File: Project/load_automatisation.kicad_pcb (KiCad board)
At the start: 2 copper layers, 263.4 x 251.4 mm, 115 parts, among them IC1 OPA2145IDR, IC10 TD62083AFGNEL, IC11 MC74VHC138DR2G, IC2 TD62083AFGNEL, IC3 TD62083AFGNEL, IC4 MC74VHC138DR2G, IC5 MC74VHC138DR2G, IC6 TD62083AFGNEL, IC7 TD62083AFGNEL, IC8 TD62083AFGNEL, IC9 OPA145IDBVT, J1 PowerNeg, J12 PH-2X05SG, J13 1757242, J30 1757349, J9 PowerIn, K1 V23079C1103B301, K10 IMC03TS, K11 V23079C1103B301, K12 V23079C1103B301, K13 V23079C1103B301, K14 IMC03TS, K15 IMC03TS, K16 IMC03TS, K17 V23079C1103B301, K18 V23079C1103B301, K19 V23079C1103B301, K2 V23079C1103B301, K20 V23079C1103B301, K21 V23079C1103B301, K22 IMC03TS, K23 IMC03TS, K24 IMC03TS, K25 IMC03TS, K26 IMC03TS, K27 V23079C1103B301, K28 V23079C1103B301, K29 V23079C1103B301, K3 V23079C1103B301, K30 IMC03TS, K31 IMC03TS, K32 IMC03TS, K33 V23079C1103B301, K34 V23079C1103B301, K35 V23079C1103B301, K36 V23079C1103B301, K37 V23079C1103B301, K38 IMC03TS, K39 IMC03TS, K4 V23079C1103B301, K40 IMC03TS, K41 IMC03TS, K42 IMC03TS, K43 V23079C1103B301, K44 V23079C1103B301, K45 V23079C1103B301, K46 IMC03TS, K47 IMC03TS, K48 IMC03TS, K5 V23079C1103B301, K6 IMC03TS, K7 IMC03TS, K8 IMC03TS, K9 IMC03TS, U1 AMS1117-5.0, U2 INA128, U3 AMS1117-5.0

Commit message: place arrangement
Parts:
- added C17: 100nF, Capacitor_SMD:C_0805_2012Metric, F.Cu at (197.2, 158.9)
- added C18: 100nF, Capacitor_SMD:C_0805_2012Metric, F.Cu at (192.3, 178.8)
- added R2: R, Resistor_SMD:R_0805_2012Metric, F.Cu at (246.9, 176.7)
- moved IC1 83.4 mm to (147.8, 268.0), turned to 0 degrees
- moved C2 70.6 mm to (157.8, 173.4)
- moved R3 35.4 mm to (186.4, 174.3), turned to 90 degrees
- moved R4 27.3 mm to (192.6, 169.4), turned to 0 degrees
- moved C5 27.2 mm to (187.5, 162.1), turned to -90 degrees
- moved U1 25.0 mm to (147.1, 171.6)
- moved C3 24.3 mm to (200.3, 174.6), turned to -90 degrees
- moved U2 21.5 mm to (192.4, 174.3), turned to 0 degrees
- moved C4 21.4 mm to (192.6, 156.6)
- moved R1 18.5 mm to (192.6, 154.4)
- moved IC9 16.2 mm to (192.4, 160.2)
- moved C1 13.7 mm to (136.4, 172.8)
- moved C16 13.2 mm to (157.8, 155.6)
- moved U3 4.14 mm to (147.2, 156.8)
- moved C15 2.17 mm to (136.7, 155.0)
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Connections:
- C6 pad 1: VCC -> VCC1
- C7 pad 1: VCC -> VCC1
- C9 pad 1: VCC -> VCC1
- IC11 pad 16: VCC -> VCC1
- IC2 pad 10: VCC -> VCC1
- IC3 pad 10: VCC -> VCC1
- J30 pad 1: unconnected-(J30-Pad1) -> /V_daq-
- J30 pad 10: /V_daq+ -> unconnected-(J30-Pad10)
- J30 pad 2: unconnected-(J30-Pad2) -> /V_daq+
- J30 pad 9: /V_daq- -> unconnected-(J30-Pad9)
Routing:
- net GND: track 1617.8 -> 1272.1 mm, vias 20 -> 14
- net VCC: track 666.4 -> 359.4 mm, vias 8 -> 4
- net -VCC: track 151.9 -> 0.00 mm, vias 8 -> 0
- net /Vsense: track 895.1 -> 784.7 mm, vias 1 -> 0
- net VCC1: track 0.00 -> 80.8 mm
- net /V_daq+: track 73.9 -> 0.00 mm
- net /Teng-: track 883.7 -> 812.5 mm, vias 1 -> 0
- net /V_daq-: track 67.0 -> 0.00 mm
- net unconnected-(J30-Pad9): track 0.00 -> 62.8 mm
- net /Current_Sense2_IN: track 73.7 -> 27.9 mm, vias 1 -> 0
- net /Vin: track 45.3 -> 0.00 mm
- net /Current_Sense1_IN: track 66.0 -> 24.2 mm
- net /Current_Sense2_OUT: track 61.0 -> 25.1 mm, vias 2 -> 1
- net /VNeg: track 23.1 -> 0.74 mm
- net /Dout2: track 83.8 -> 68.4 mm
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- removed copper zone on F.Cu, net VCC

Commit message: routing 11/12
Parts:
- added C19: 100nF, Capacitor_SMD:C_0805_2012Metric, F.Cu at (162.8, 247.1)
- added C20: 100nF, Capacitor_SMD:C_0805_2012Metric, F.Cu at (192.0, 163.5)
- added R5: R, Resistor_SMD:R_0805_2012Metric, F.Cu at (270.7, 254.7)
- added R6: R, Resistor_SMD:R_0805_2012Metric, F.Cu at (214.5, 243.1)
- moved C12 104.8 mm to (310.3, 258.8), turned to 180 degrees
- moved C13 89.4 mm to (208.2, 281.9), turned to 90 degrees
- moved C8 87.4 mm to (225.8, 281.4), turned to 90 degrees
- moved C5 81.5 mm to (155.8, 237.1), turned to 90 degrees
- moved C14 78.5 mm to (311.5, 241.4), turned to 180 degrees
- moved C11 74.8 mm to (283.3, 233.5), turned to 180 degrees
- moved C10 74.7 mm to (234.0, 253.6), turned to 90 degrees
- moved IC1 29.4 mm to (159.8, 241.0), turned to 90 degrees
- moved C3 2.37 mm to (198.8, 172.7), turned to 90 degrees
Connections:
- C10 pad 1: VCC -> VCC3
- C11 pad 1: VCC -> VCC2
- C12 pad 1: VCC -> VCC2
- C13 pad 1: VCC -> VCC3
- C14 pad 1: VCC -> VCC2
- C8 pad 1: VCC -> VCC3
- IC10 pad 10: VCC -> VCC3
- IC4 pad 16: VCC -> VCC2
- IC5 pad 16: VCC -> VCC3
- IC6 pad 10: VCC -> VCC2
- IC7 pad 10: VCC -> VCC2
- IC8 pad 10: VCC -> VCC3
- J30 pad 1: /V_daq- -> /V_daq+
- J30 pad 11: /Dout2 -> /Dout1
- J30 pad 12: /Dout1 -> /Dout2
- J30 pad 2: /V_daq+ -> /V_daq-
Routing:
- net GND: track 1272.1 -> 1644.3 mm, vias 14 -> 18
- net -VCC: track 0.00 -> 210.5 mm, vias 0 -> 4
- net VCC2: track 0.00 -> 126.3 mm
- net VCC3: track 0.00 -> 104.4 mm, vias 0 -> 2
- net /Teng-: track 812.5 -> 884.9 mm, vias 0 -> 1
- net unconnected-(J30-Pad9): track 62.8 -> 0.00 mm
- net /Vsense: track 784.7 -> 823.7 mm, vias 0 -> 1
- net VCC: track 359.4 -> 325.1 mm, vias 4 -> 5
- net /V_daq-: track 0.00 -> 33.7 mm
- net /V_daq+: track 0.00 -> 30.6 mm
- net /Vin: track 0.00 -> 20.8 mm
- net /VNeg: track 0.74 -> 20.6 mm
- net /Dout1: track 115.1 -> 133.8 mm
- net /Dout2: track 68.4 -> 76.6 mm
- net VCC1: track 80.8 -> 85.1 mm
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
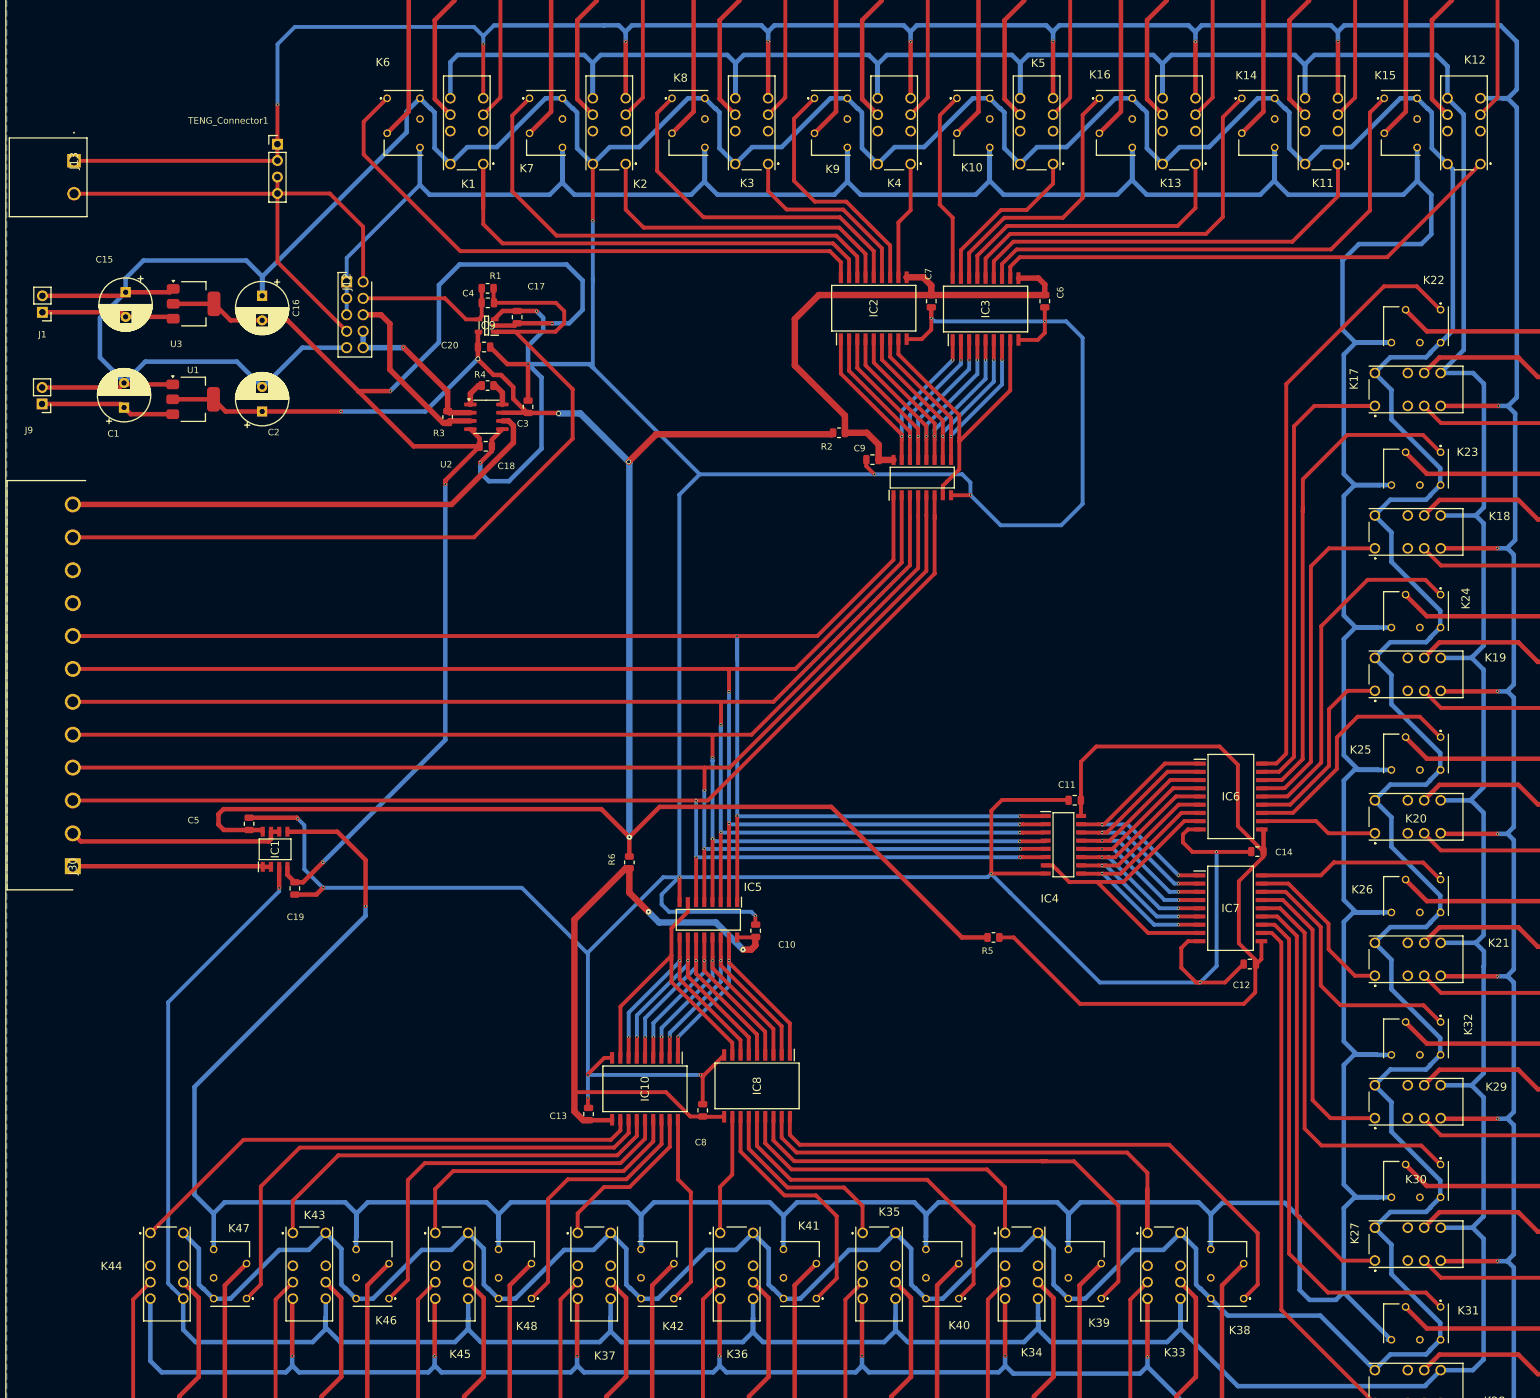
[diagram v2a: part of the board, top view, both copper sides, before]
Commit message: new routing 12/12
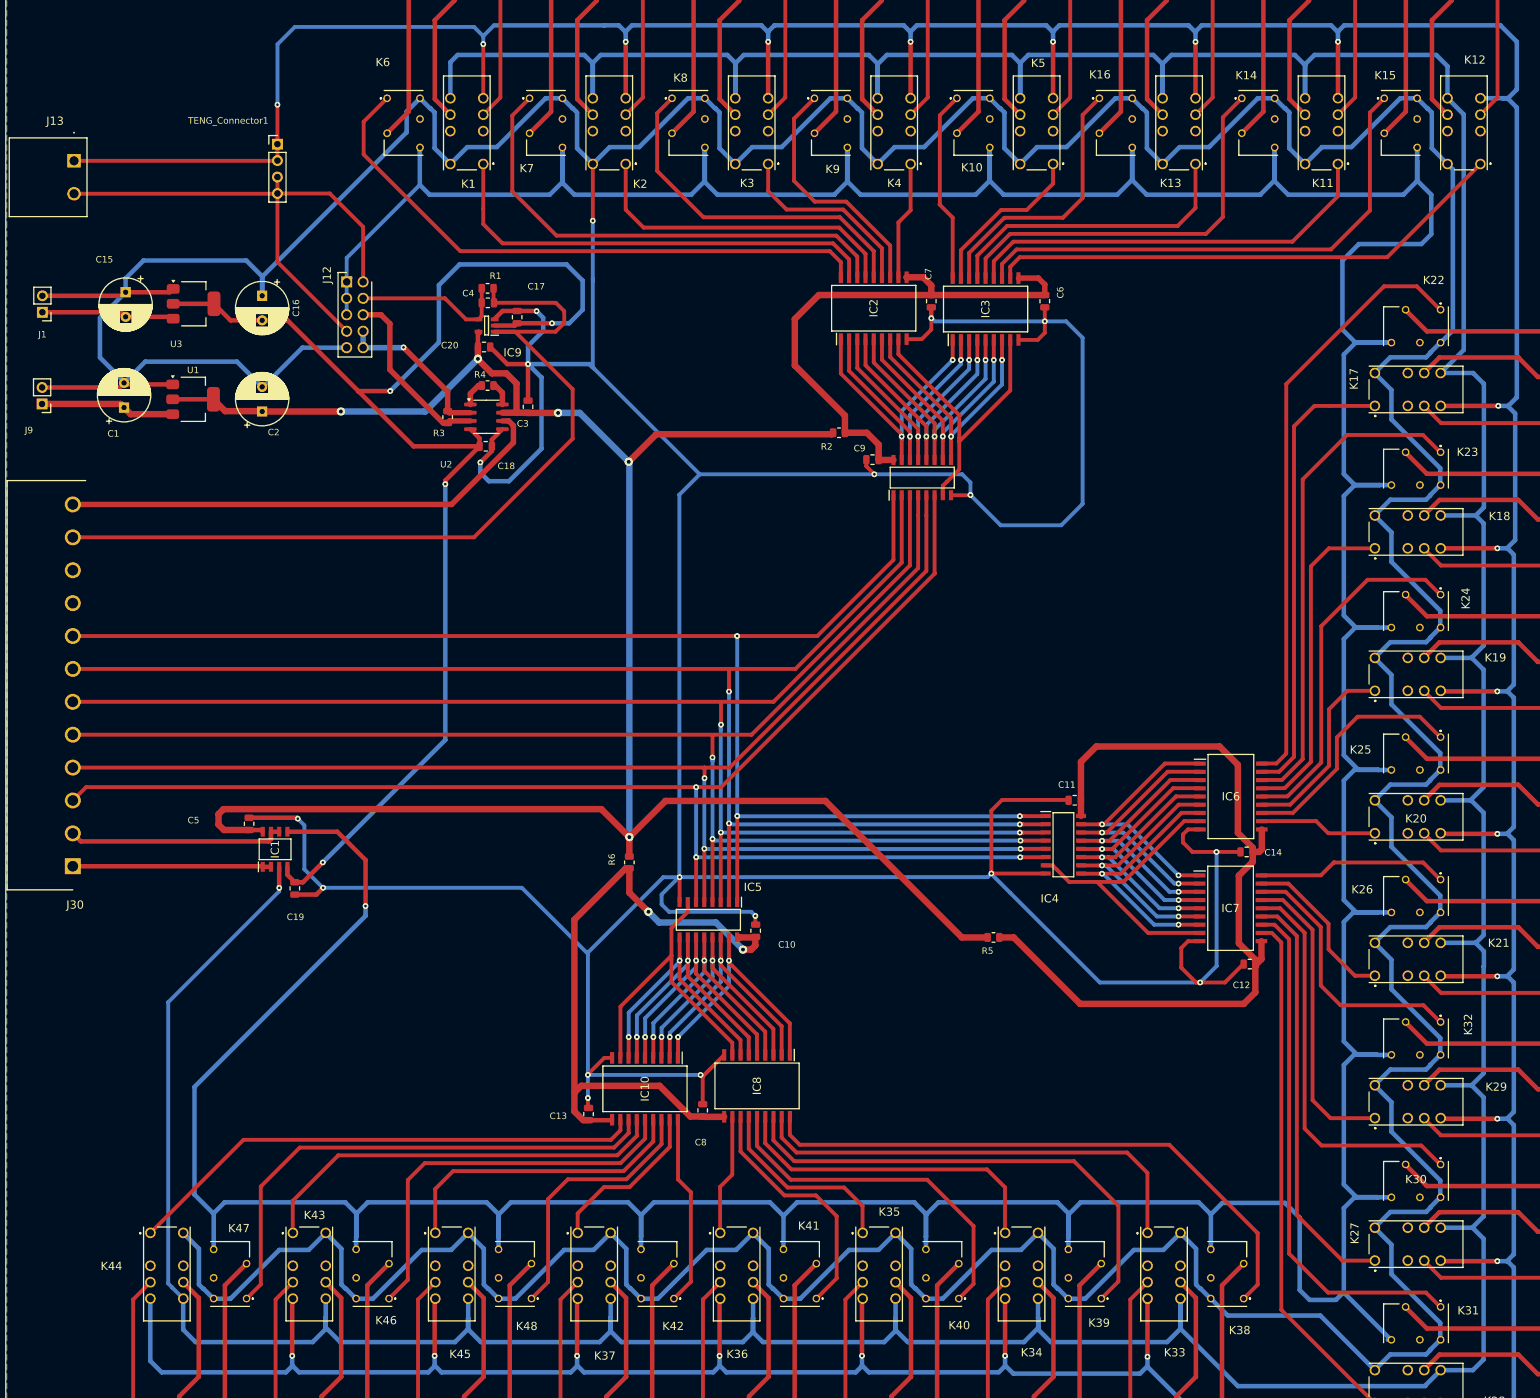
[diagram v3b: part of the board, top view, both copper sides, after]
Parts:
- moved C14 1.66 mm to (309.8, 241.5)
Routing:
- net /3_Loads/O34: track 77.7 -> 70.8 mm
- net /2_Loads/O18: track 77.7 -> 70.8 mm
- net /1_Loads/O2: track 77.7 -> 70.8 mm
- net /Din0: track 233.6 -> 230.0 mm
- net /Din5: track 229.0 -> 231.1 mm
- net GND: track 1644.3 -> 1642.6 mm
- net VCC1: track 85.1 -> 83.6 mm
- net /3_Loads/O35: track 76.8 -> 76.1 mm
- net /2_Loads/O19: track 76.8 -> 76.1 mm
- net VCC: track 325.1 -> 325.6 mm

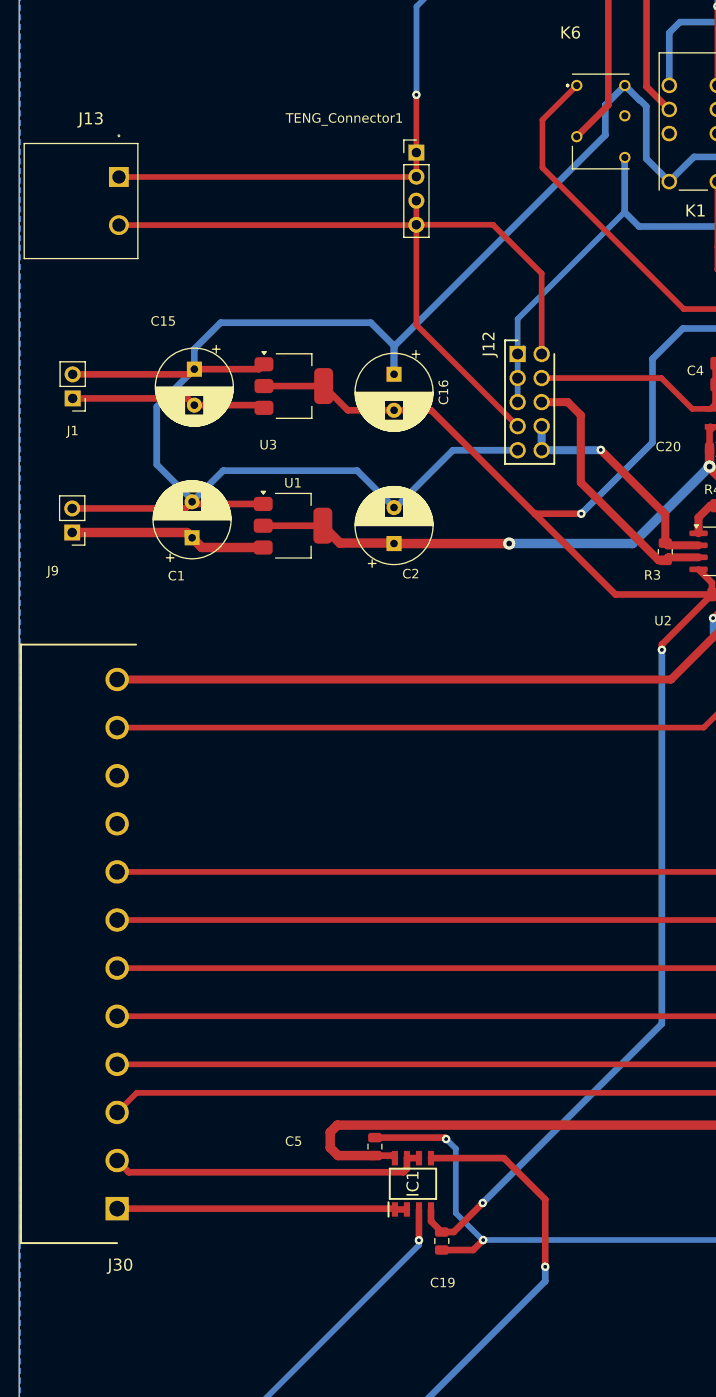
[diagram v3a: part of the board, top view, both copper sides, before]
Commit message: new routing 12/12
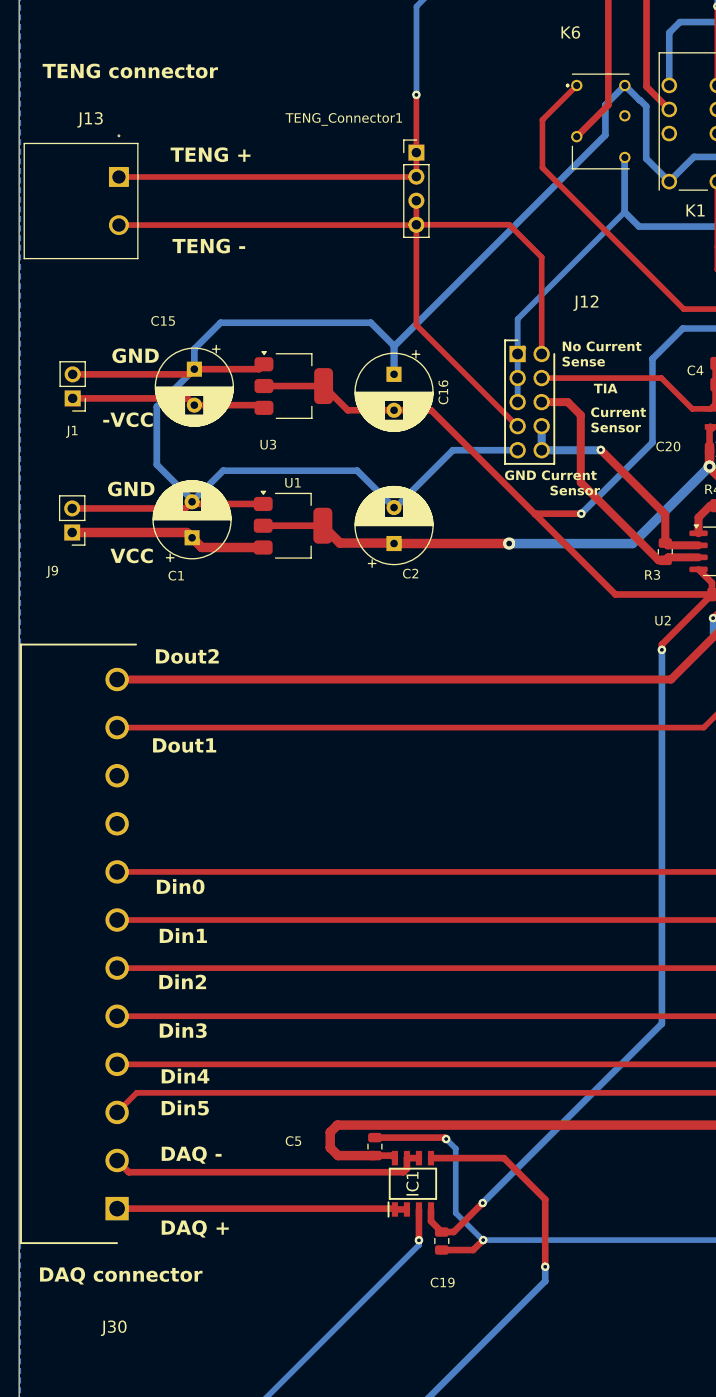
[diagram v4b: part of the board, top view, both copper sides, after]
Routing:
- net /TengN: track 83.5 -> 84.6 mm
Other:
- board text added: "-VCC"
- board text added: "Current Sensor"
- board text added: "DAQ +"
- board text added: "DAQ -"
- board text added: "DAQ connector"
- board text added: "Din0"
- board text added: "Din1"
- board text added: "Din2"
- board text added: "Din3"
- board text added: "Din4"
- board text added: "Din5"
- board text added: "Dout1"
- board text added: "Dout2"
- board text added: "GND"
- board text added: "GND Current Sensor"
- board text added: "No Current Sense"
- board text added: "TENG +"
- board text added: "TENG -"
- board text added: "TENG connector"
- board text added: "TIA"
- board text added: "VCC"

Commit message: new 16/01
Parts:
- added TENG_Connector2: Conn_01x04_Pin, Connector_PinHeader_2.54mm:PinHeader_1x04_P2.54mm_Vertical, F.Cu at (164.7, 132.1)
- moved C5 1.93 mm to (156.4, 235.3), turned to 180 degrees
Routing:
- net VCC: track 325.6 -> 352.2 mm
- net -VCC: track 210.5 -> 185.0 mm
- net /TengN: track 84.6 -> 78.8 mm
- net /Teng-: track 884.9 -> 882.4 mm
